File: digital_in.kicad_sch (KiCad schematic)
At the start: 24 parts, among them U1401 CDSOT236-T05, U1402 AM26LV32E, U1403 CDSOT236-T05

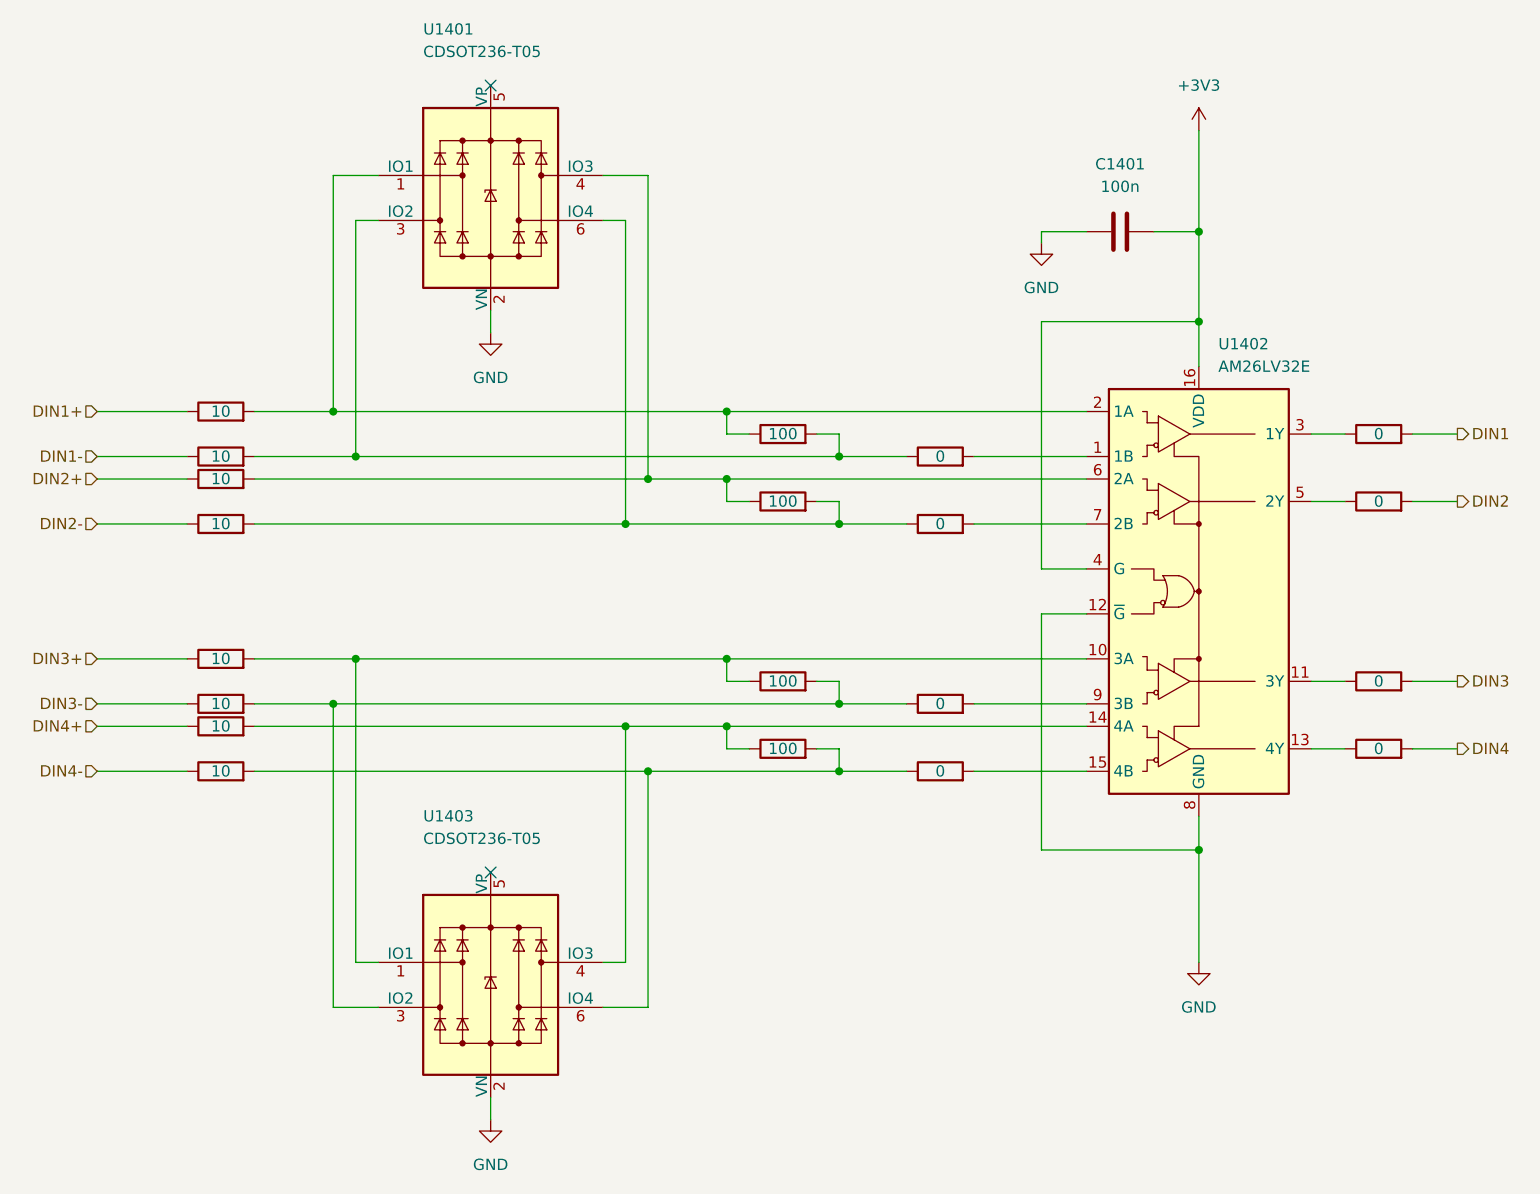
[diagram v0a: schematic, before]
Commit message: Split schematic into three subprojects
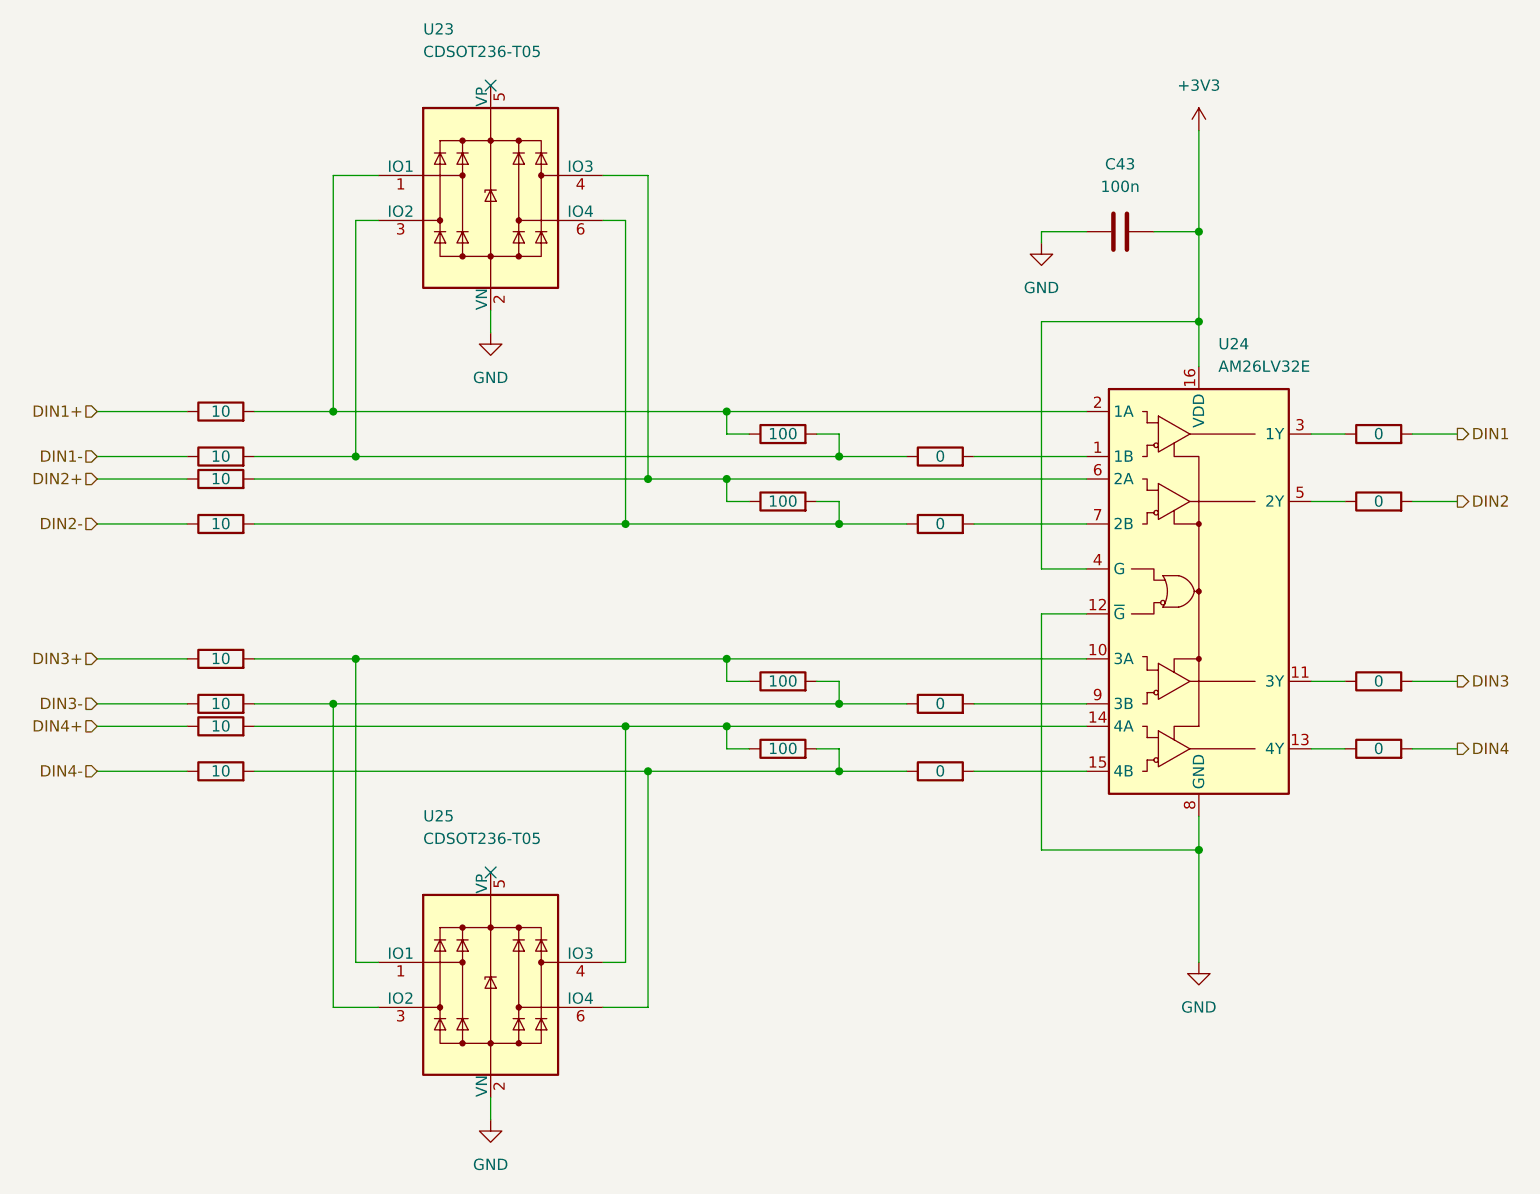
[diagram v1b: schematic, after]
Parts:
- renumbered C1401 to C43, R1401 to R146, R1402 to R147, R1103 to R148, R1404 to R149, R1105 to R150, R1406 to R151, R1407 to R152, R1108 to R153, R1409 to R154, R1110 to R155, R1411 to R156, R1412 to R157, R1113 to R158, R1414 to R159, R1115 to R160, R1416 to R161, R1417 to R162, R1118 to R163, R1419 to R164, R1120 to R165, U1401 to U23, U1402 to U24, U1403 to U25

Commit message: Updated designators positions
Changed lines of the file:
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@@
   (symbol (lib_id "Device:R") (at 102.87 118.11 90) (unit 1)
     (in_bom yes) (on_board yes) (dnp no)
-    (property "Reference" "R164" (at 102.87 111.76 90)
-      (effects (font (size 1.27 1.27)) hide)
+    (property "Reference" "R164" (at 107.95 116.84 90)
+      (effects (font (size 1.27 1.27)))
     )
     (property "Value" "10" (at 102.87 118.11 90)
@@
   (symbol (lib_id "Device:R") (at 233.68 115.57 90) (unit 1)
     (in_bom yes) (on_board yes) (dnp no)
-    (property "Reference" "R163" (at 233.68 109.22 90)
-      (effects (font (size 1.27 1.27)) hide)
+    (property "Reference" "R163" (at 233.68 113.538 90)
+      (effects (font (size 1.27 1.27)))
     )
     (property "Value" "0" (at 233.68 115.57 90)
@@
   (symbol (lib_id "Device:R") (at 102.87 105.41 90) (unit 1)
     (in_bom yes) (on_board yes) (dnp no)
-    (property "Reference" "R156" (at 102.87 99.06 90)
-      (effects (font (size 1.27 1.27)) hide)
+    (property "Reference" "R156" (at 107.95 104.14 90)
+      (effects (font (size 1.27 1.27)))
     )
     (property "Value" "10" (at 102.87 105.41 90)
@@
   (symbol (lib_id "Device:R") (at 102.87 110.49 90) (unit 1)
     (in_bom yes) (on_board yes) (dnp no)
-    (property "Reference" "R159" (at 102.87 104.14 90)
-      (effects (font (size 1.27 1.27)) hide)
+    (property "Reference" "R159" (at 107.95 109.22 90)
+      (effects (font (size 1.27 1.27)))
     )
     (property "Value" "10" (at 102.87 110.49 90)
@@
   (symbol (lib_id "Device:R") (at 184.15 82.55 90) (unit 1)
     (in_bom yes) (on_board yes) (dnp no)
-    (property "Reference" "R150" (at 184.15 76.2 90)
-      (effects (font (size 1.27 1.27)) hide)
+    (property "Reference" "R150" (at 184.15 80.518 90)
+      (effects (font (size 1.27 1.27)))
     )
     (property "Value" "0" (at 184.15 82.55 90)
@@
   (symbol (lib_id "Device:R") (at 233.68 107.95 90) (unit 1)
     (in_bom yes) (on_board yes) (dnp no)
-    (property "Reference" "R158" (at 233.68 101.6 90)
-      (effects (font (size 1.27 1.27)) hide)
+    (property "Reference" "R158" (at 233.68 105.918 90)
+      (effects (font (size 1.27 1.27)))
     )
     (property "Value" "0" (at 233.68 107.95 90)
@@
   (symbol (lib_id "Device:R") (at 102.87 90.17 90) (unit 1)
     (in_bom yes) (on_board yes) (dnp no)
-    (property "Reference" "R154" (at 102.87 83.82 90)
-      (effects (font (size 1.27 1.27)) hide)
+    (property "Reference" "R154" (at 107.95 88.9 90)
+      (effects (font (size 1.27 1.27)))
     )
     (property "Value" "10" (at 102.87 90.17 90)
@@
   (symbol (lib_id "Device:R") (at 102.87 113.03 90) (unit 1)
     (in_bom yes) (on_board yes) (dnp no)
-    (property "Reference" "R161" (at 102.87 106.68 90)
-      (effects (font (size 1.27 1.27)) hide)
+    (property "Reference" "R161" (at 107.95 111.76 90)
+      (effects (font (size 1.27 1.27)))
     )
     (property "Value" "10" (at 102.87 113.03 90)
@@
   (symbol (lib_id "Device:R") (at 166.37 107.95 90) (unit 1)
     (in_bom yes) (on_board yes) (dnp no)
-    (property "Reference" "R157" (at 166.37 101.6 90)
-      (effects (font (size 1.27 1.27)) hide)
+    (property "Reference" "R157" (at 171.45 106.68 90)
+      (effects (font (size 1.27 1.27)))
     )
     (property "Value" "100" (at 166.37 107.95 90)
@@
   (symbol (lib_id "Device:R") (at 166.37 87.63 90) (unit 1)
     (in_bom yes) (on_board yes) (dnp no)
-    (property "Reference" "R152" (at 166.37 81.28 90)
-      (effects (font (size 1.27 1.27)) hide)
+    (property "Reference" "R152" (at 171.45 86.36 90)
+      (effects (font (size 1.27 1.27)))
     )
     (property "Value" "100" (at 166.37 87.63 90)
@@
   (symbol (lib_id "Device:R") (at 184.15 90.17 90) (unit 1)
     (in_bom yes) (on_board yes) (dnp no)
-    (property "Reference" "R155" (at 184.15 83.82 90)
-      (effects (font (size 1.27 1.27)) hide)
+    (property "Reference" "R155" (at 184.15 88.138 90)
+      (effects (font (size 1.27 1.27)))
     )
     (property "Value" "0" (at 184.15 90.17 90)
@@
   (symbol (lib_id "Device:R") (at 166.37 115.57 90) (unit 1)
     (in_bom yes) (on_board yes) (dnp no)
-    (property "Reference" "R162" (at 166.37 109.22 90)
-      (effects (font (size 1.27 1.27)) hide)
+    (property "Reference" "R162" (at 171.45 114.3 90)
+      (effects (font (size 1.27 1.27)))
     )
     (property "Value" "100" (at 166.37 115.57 90)
@@
   (symbol (lib_id "Device:R") (at 102.87 85.09 90) (unit 1)
     (in_bom yes) (on_board yes) (dnp no)
-    (property "Reference" "R151" (at 102.87 78.74 90)
-      (effects (font (size 1.27 1.27)) hide)
+    (property "Reference" "R151" (at 107.95 83.82 90)
+      (effects (font (size 1.27 1.27)))
     )
     (property "Value" "10" (at 102.87 85.09 90)
@@
   (symbol (lib_id "Device:R") (at 233.68 80.01 90) (unit 1)
     (in_bom yes) (on_board yes) (dnp no)
-    (property "Reference" "R148" (at 233.68 73.66 90)
-      (effects (font (size 1.27 1.27)) hide)
+    (property "Reference" "R148" (at 233.68 77.978 90)
+      (effects (font (size 1.27 1.27)))
     )
     (property "Value" "0" (at 233.68 80.01 90)
@@
   (symbol (lib_id "Device:R") (at 166.37 80.01 90) (unit 1)
     (in_bom yes) (on_board yes) (dnp no)
-    (property "Reference" "R147" (at 166.37 73.66 90)
-      (effects (font (size 1.27 1.27)) hide)
+    (property "Reference" "R147" (at 171.45 78.74 90)
+      (effects (font (size 1.27 1.27)))
     )
     (property "Value" "100" (at 166.37 80.01 90)
@@
   (symbol (lib_id "Device:R") (at 102.87 77.47 90) (unit 1)
     (in_bom yes) (on_board yes) (dnp no)
-    (property "Reference" "R146" (at 102.87 71.12 90)
-      (effects (font (size 1.27 1.27)) hide)
+    (property "Reference" "R146" (at 107.95 76.2 90)
+      (effects (font (size 1.27 1.27)))
     )
     (property "Value" "10" (at 102.87 77.47 90)
@@
   (symbol (lib_id "Device:R") (at 184.15 118.11 90) (unit 1)
     (in_bom yes) (on_board yes) (dnp no)
-    (property "Reference" "R165" (at 184.15 111.76 90)
-      (effects (font (size 1.27 1.27)) hide)
+    (property "Reference" "R165" (at 184.15 116.078 90)
+      (effects (font (size 1.27 1.27)))
     )
     (property "Value" "0" (at 184.15 118.11 90)
@@
   (symbol (lib_id "Device:R") (at 184.15 110.49 90) (unit 1)
     (in_bom yes) (on_board yes) (dnp no)
-    (property "Reference" "R160" (at 184.15 104.14 90)
-      (effects (font (size 1.27 1.27)) hide)
+    (property "Reference" "R160" (at 184.15 108.458 90)
+      (effects (font (size 1.27 1.27)))
     )
     (property "Value" "0" (at 184.15 110.49 90)
@@
   (symbol (lib_id "Device:R") (at 102.87 82.55 90) (unit 1)
     (in_bom yes) (on_board yes) (dnp no)
-    (property "Reference" "R149" (at 102.87 76.2 90)
-      (effects (font (size 1.27 1.27)) hide)
+    (property "Reference" "R149" (at 107.95 81.28 90)
+      (effects (font (size 1.27 1.27)))
     )
     (property "Value" "10" (at 102.87 82.55 90)
@@
   (symbol (lib_id "Device:R") (at 233.68 87.63 90) (unit 1)
     (in_bom yes) (on_board yes) (dnp no)
-    (property "Reference" "R153" (at 233.68 81.28 90)
-      (effects (font (size 1.27 1.27)) hide)
+    (property "Reference" "R153" (at 233.68 85.598 90)
+      (effects (font (size 1.27 1.27)))
     )
     (property "Value" "0" (at 233.68 87.63 90)

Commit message: Set capacitor and resistor values on tranciever circuits
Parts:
- C43: value 100n -> 100nF
- R148, R150, R153, R155, R158, R160, R163, R165: value 0 -> 0R
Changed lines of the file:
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@@
       (effects (font (size 1.27 1.27)) hide)
     )
-    (property "Datasheet" "~" (at 102.87 118.11 0)
+    (property "Datasheet" "10Ω 75V Thick Film 1%" (at 102.87 118.11 0)
       (effects (font (size 1.27 1.27)) hide)
     )
@@
       (effects (font (size 1.27 1.27)))
     )
-    (property "Value" "100n" (at 204.47 52.07 90)
+    (property "Value" "100nF" (at 204.47 52.07 90)
       (effects (font (size 1.27 1.27)))
     )
@@
       (effects (font (size 1.27 1.27)) hide)
     )
-    (property "Datasheet" "~" (at 204.47 57.15 0)
+    (property "Datasheet" "100nF 50V X7R 10%" (at 204.47 57.15 0)
       (effects (font (size 1.27 1.27)) hide)
     )
@@
       (effects (font (size 1.27 1.27)))
     )
-    (property "Value" "0" (at 233.68 115.57 90)
+    (property "Value" "0R" (at 233.68 115.57 90)
       (effects (font (size 1.27 1.27)))
     )
@@
       (effects (font (size 1.27 1.27)) hide)
     )
-    (property "Datasheet" "~" (at 233.68 115.57 0)
+    (property "Datasheet" "0Ω 75V Thick Film 1%" (at 233.68 115.57 0)
       (effects (font (size 1.27 1.27)) hide)
     )
@@
       (effects (font (size 1.27 1.27)) hide)
     )
-    (property "Datasheet" "~" (at 102.87 105.41 0)
+    (property "Datasheet" "10Ω 75V Thick Film 1%" (at 102.87 105.41 0)
       (effects (font (size 1.27 1.27)) hide)
     )
@@
       (effects (font (size 1.27 1.27)) hide)
     )
-    (property "Datasheet" "~" (at 102.87 110.49 0)
+    (property "Datasheet" "10Ω 75V Thick Film 1%" (at 102.87 110.49 0)
       (effects (font (size 1.27 1.27)) hide)
     )
@@
       (effects (font (size 1.27 1.27)))
     )
-    (property "Value" "0" (at 184.15 82.55 90)
+    (property "Value" "0R" (at 184.15 82.55 90)
       (effects (font (size 1.27 1.27)))
     )
@@
       (effects (font (size 1.27 1.27)) hide)
     )
-    (property "Datasheet" "~" (at 184.15 82.55 0)
+    (property "Datasheet" "0Ω 75V Thick Film 1%" (at 184.15 82.55 0)
       (effects (font (size 1.27 1.27)) hide)
     )
@@
       (effects (font (size 1.27 1.27)))
     )
-    (property "Value" "0" (at 233.68 107.95 90)
+    (property "Value" "0R" (at 233.68 107.95 90)
       (effects (font (size 1.27 1.27)))
     )
@@
       (effects (font (size 1.27 1.27)) hide)
     )
-    (property "Datasheet" "~" (at 233.68 107.95 0)
+    (property "Datasheet" "0Ω 75V Thick Film 1%" (at 233.68 107.95 0)
       (effects (font (size 1.27 1.27)) hide)
     )
@@
       (effects (font (size 1.27 1.27)) hide)
     )
-    (property "Datasheet" "~" (at 102.87 90.17 0)
+    (property "Datasheet" "10Ω 75V Thick Film 1%" (at 102.87 90.17 0)
       (effects (font (size 1.27 1.27)) hide)
     )
@@
       (effects (font (size 1.27 1.27)) hide)
     )
-    (property "Datasheet" "~" (at 102.87 113.03 0)
+    (property "Datasheet" "10Ω 75V Thick Film 1%" (at 102.87 113.03 0)
       (effects (font (size 1.27 1.27)) hide)
     )
@@
       (effects (font (size 1.27 1.27)) hide)
     )
-    (property "Datasheet" "~" (at 166.37 107.95 0)
+    (property "Datasheet" "100Ω 75V Thick Film 1%" (at 166.37 107.95 0)
       (effects (font (size 1.27 1.27)) hide)
     )
@@
       (effects (font (size 1.27 1.27)) hide)
     )
-    (property "Datasheet" "~" (at 166.37 87.63 0)
+    (property "Datasheet" "100Ω 75V Thick Film 1%" (at 166.37 87.63 0)
       (effects (font (size 1.27 1.27)) hide)
     )
@@
       (effects (font (size 1.27 1.27)))
     )
-    (property "Value" "0" (at 184.15 90.17 90)
+    (property "Value" "0R" (at 184.15 90.17 90)
       (effects (font (size 1.27 1.27)))
     )
@@
       (effects (font (size 1.27 1.27)) hide)
     )
-    (property "Datasheet" "~" (at 184.15 90.17 0)
+    (property "Datasheet" "0Ω 75V Thick Film 1%" (at 184.15 90.17 0)
       (effects (font (size 1.27 1.27)) hide)
     )
@@
       (effects (font (size 1.27 1.27)) hide)
     )
-    (property "Datasheet" "~" (at 166.37 115.57 0)
+    (property "Datasheet" "100Ω 75V Thick Film 1%" (at 166.37 115.57 0)
       (effects (font (size 1.27 1.27)) hide)
     )
@@
       (effects (font (size 1.27 1.27)) hide)
     )
-    (property "Datasheet" "~" (at 102.87 85.09 0)
+    (property "Datasheet" "10Ω 75V Thick Film 1%" (at 102.87 85.09 0)
       (effects (font (size 1.27 1.27)) hide)
     )
@@
       (effects (font (size 1.27 1.27)))
     )
-    (property "Value" "0" (at 233.68 80.01 90)
+    (property "Value" "0R" (at 233.68 80.01 90)
       (effects (font (size 1.27 1.27)))
     )
@@
       (effects (font (size 1.27 1.27)) hide)
     )
-    (property "Datasheet" "~" (at 233.68 80.01 0)
+    (property "Datasheet" "0Ω 75V Thick Film 1%" (at 233.68 80.01 0)
       (effects (font (size 1.27 1.27)) hide)
     )
@@
       (effects (font (size 1.27 1.27)) hide)
     )
-    (property "Datasheet" "~" (at 166.37 80.01 0)
+    (property "Datasheet" "100Ω 75V Thick Film 1%" (at 166.37 80.01 0)
       (effects (font (size 1.27 1.27)) hide)
     )
@@
       (effects (font (size 1.27 1.27)) hide)
     )
-    (property "Datasheet" "~" (at 102.87 77.47 0)
+    (property "Datasheet" "10Ω 75V Thick Film 1%" (at 102.87 77.47 0)
       (effects (font (size 1.27 1.27)) hide)
     )
@@
       (effects (font (size 1.27 1.27)))
     )
-    (property "Value" "0" (at 184.15 118.11 90)
+    (property "Value" "0R" (at 184.15 118.11 90)
       (effects (font (size 1.27 1.27)))
     )
@@
       (effects (font (size 1.27 1.27)) hide)
     )
-    (property "Datasheet" "~" (at 184.15 118.11 0)
+    (property "Datasheet" "0Ω 75V Thick Film 1%" (at 184.15 118.11 0)
       (effects (font (size 1.27 1.27)) hide)
     )
@@
       (effects (font (size 1.27 1.27)))
     )
-    (property "Value" "0" (at 184.15 110.49 90)
+    (property "Value" "0R" (at 184.15 110.49 90)
       (effects (font (size 1.27 1.27)))
     )
@@
       (effects (font (size 1.27 1.27)) hide)
     )
-    (property "Datasheet" "~" (at 184.15 110.49 0)
+    (property "Datasheet" "0Ω 75V Thick Film 1%" (at 184.15 110.49 0)
       (effects (font (size 1.27 1.27)) hide)
     )
@@
       (effects (font (size 1.27 1.27)) hide)
     )
-    (property "Datasheet" "~" (at 102.87 82.55 0)
+    (property "Datasheet" "10Ω 75V Thick Film 1%" (at 102.87 82.55 0)
       (effects (font (size 1.27 1.27)) hide)
     )
@@
       (effects (font (size 1.27 1.27)))
     )
-    (property "Value" "0" (at 233.68 87.63 90)
+    (property "Value" "0R" (at 233.68 87.63 90)
       (effects (font (size 1.27 1.27)))
     )
@@
       (effects (font (size 1.27 1.27)) hide)
     )
-    (property "Datasheet" "~" (at 233.68 87.63 0)
-      (effects (font (size 1.27 1.27)) hide)
-    )
+    (property "Datasheet" "0Ω 75V Thick Film 1%" (at 233.68 87.63 0)
+      (effects (font (size 1.27 1.27)) hide)
+    )

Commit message: Assigned footprints for digital components
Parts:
- removed R146, R149, R151, R154, R156, R159, R161, R164: 10, Resistor_SMD:R_0603_1608Metric_Pad0.98x0.95mm_HandSolder, symbol Device:R
- removed R150, R155, R160, R165: 0R, Resistor_SMD:R_0603_1608Metric_Pad0.98x0.95mm_HandSolder, symbol Device:R
- added R26, R29, R30, R33, R34, R37, R38, R41: 10, Resistor_SMD:R_0603_1608Metric_Pad0.98x0.95mm_HandSolder, symbol Device:R
- U23, U25: value CDSOT236-T05 -> SRV05-4
- renumbered R147 to R123, R148 to R124, R152 to R127, R153 to R128, R157 to R131, R158 to R132, R162 to R135, R163 to R136
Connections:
- net DIN1+: now also R123.1, U23.1 (IO1), R26.1
- net DIN1-: now also R123.2, U23.3 (IO2), R29.1
- net DIN2+: now also R127.1, U23.4 (IO3), R30.1
- net DIN2-: now also R127.2, U23.6 (IO4), R33.1
- net DIN3+: now also R131.1, U25.1 (IO1), R34.1
- net DIN3-: now also R131.2, U25.3 (IO2), R37.1
- net DIN4+: now also R135.1, U25.4 (IO3), R38.1
- net DIN4-: now also R135.2, U25.6 (IO4), R41.1
- net at U24.1 (1B): now also R29.2
- net at U24.15 (4B): now also R41.2
- net at U24.7 (2B): now also R33.2
- net at U24.9 (3B): now also R37.2
- new net: R26.2, U24.2 (1A)
- new net: R34.2, U24.10 (3A)
- new net: R38.2, U24.14 (4A)
- new net: R30.2, U24.6 (2A)
